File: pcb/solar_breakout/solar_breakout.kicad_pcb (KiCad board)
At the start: 2 copper layers, 20.8 x 43.7 mm, 25 parts, among them IC1 LTC3105, J1 CONN_01x02, J2 CONN_01x02, J3 CONN_01x02, J4 CONN_01x02, J5 CONN_01x02, J6 CONN_01x02

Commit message: Fix some stuff with the PCB
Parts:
- moved C6 4.84 mm to (151.3, 119.0), turned to 270 degrees
- moved G*** 4.67 mm to (145.2, 121.0)
- moved J1 4.32 mm to (148.6, 124.6)
- moved D2 3.95 mm to (143.8, 125.0), turned to 0 degrees
- moved L1 2.59 mm to (153.2, 123.2)
- moved IC1 2.52 mm to (148.0, 118.6)
- moved R1 2.33 mm to (145.3, 121.7)
- moved C2 2.25 mm to (148.9, 121.0)
- moved C5 2.16 mm to (145.3, 118.6)
- moved C3 2.09 mm to (150.2, 115.7), turned to 0 degrees
- moved C4 2.01 mm to (145.3, 116.2)
- moved R4 1.82 mm to (154.2, 111.5)
- moved J6 1.02 mm to (150.1, 111.3)
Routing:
- net /Panel_V: track 81.0 -> 60.9 mm
- net Net-(IC1-Pad7): track 7.71 -> 9.92 mm
- net GND: track 15.1 -> 17.0 mm
- net Net-(C3-Pad1): track 3.45 -> 1.94 mm
- net Net-(C4-Pad1): track 33.2 -> 34.7 mm
- net /D_anode: track 24.8 -> 23.4 mm
- net Net-(J6-Pad1): track 4.02 -> 5.45 mm
- net /Array_1_+: track 5.38 -> 4.15 mm
- net /Cap_V: track 67.1 -> 68.2 mm
- net Net-(C5-Pad1): track 1.77 -> 1.26 mm
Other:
- board size 20.8 x 43.7 mm -> 20.8 x 39 mm
- net class Power added: clearance 0.2, trace_width 0.3, via_dia 0.8, via_drill 0.4
- board text removed: "Feb 2019"
- board text removed: "Joel Mayer"
- board text removed: "Version 1"
- board text removed: "http://www.cusf.co.uk/"

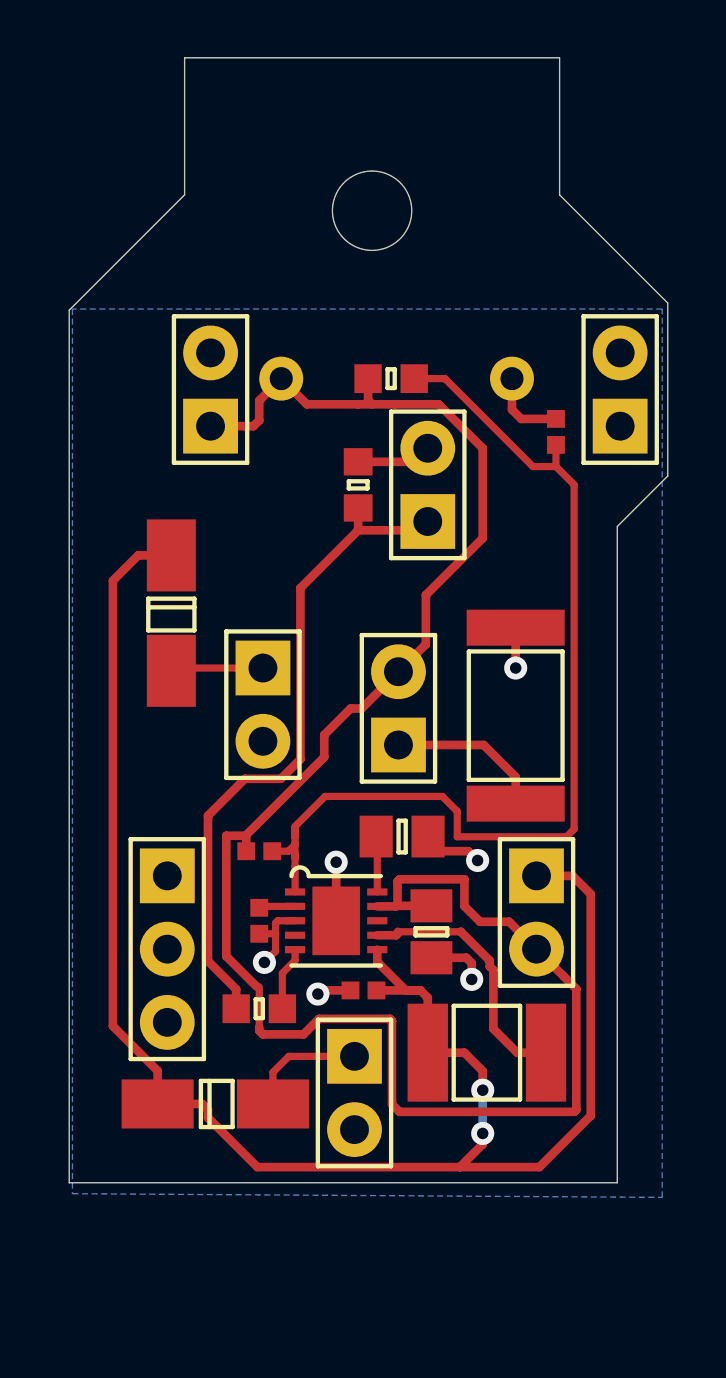
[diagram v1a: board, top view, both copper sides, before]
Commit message: Make the baord smaller and fix power lines
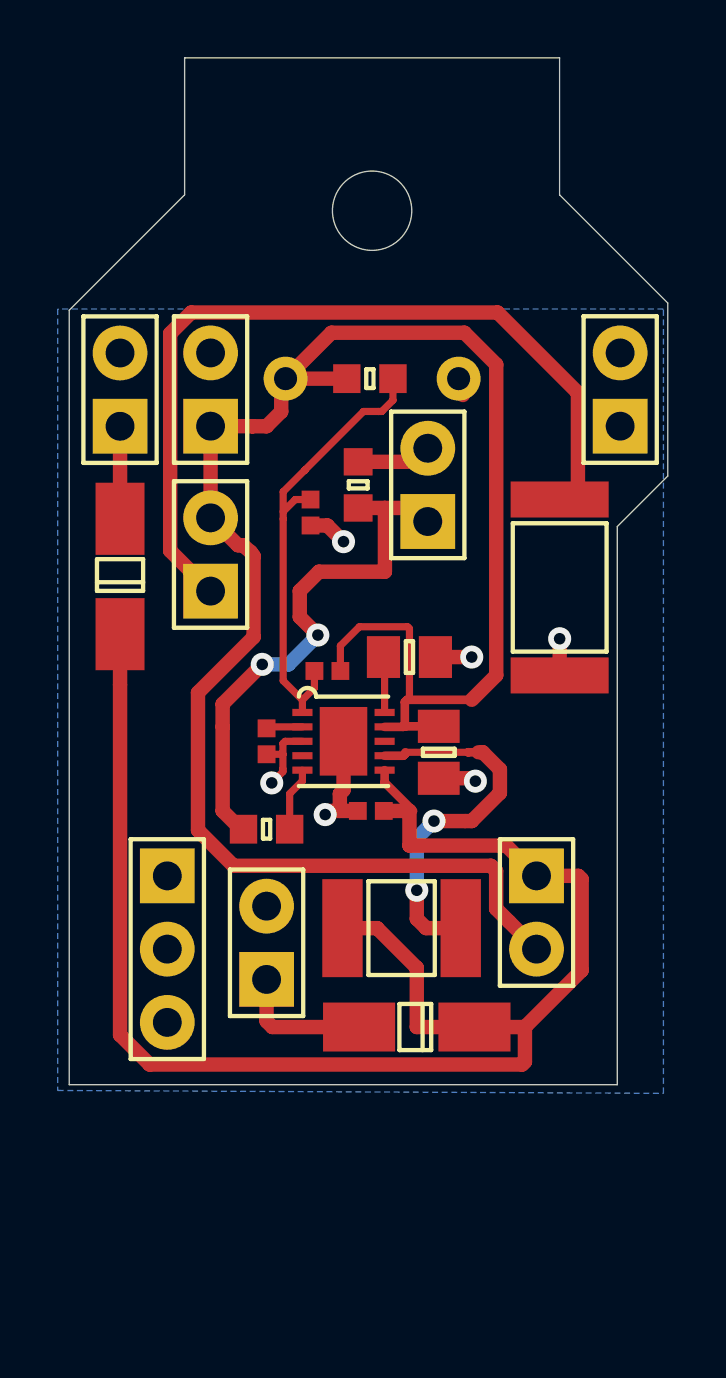
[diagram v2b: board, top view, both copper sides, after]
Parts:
- R1: value 30k -> 76.8k
- moved G*** 13.1 mm to (146.6, 108.0)
- moved J2 12.0 mm to (140.5, 100.2), turned to 90 degrees
- moved R3 8.96 mm to (147.1, 104.5), turned to 270 degrees
- moved J6 8.42 mm to (143.6, 105.9)
- moved D2 7.48 mm to (150.7, 122.3), turned to 180 degrees
- moved C4 6.68 mm to (147.7, 110.0), turned to 0 degrees
- moved C2 6.23 mm to (149.2, 114.8)
- moved C3 6.23 mm to (150.5, 109.5)
- moved C5 6.23 mm to (145.5, 112.4)
- moved C6 6.23 mm to (151.5, 112.8)
- moved IC1 6.23 mm to (148.2, 112.4)
- moved R1 6.23 mm to (145.5, 115.4)
- moved J1 6.03 mm to (145.5, 119.4), turned to 90 degrees
- moved L1 5.23 mm to (150.2, 118.9)
- moved C7 4.85 mm to (149.2, 99.8)
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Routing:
- net Net-(J6-Pad1): track 5.45 -> 28.9 mm
- net Net-(C4-Pad1): track 34.7 -> 16.1 mm
- net /Panel_V: track 60.9 -> 54.9 mm, vias 2 -> 0
- net /D_anode: track 23.4 -> 19.0 mm, vias 0 -> 2
- net Net-(IC1-Pad7): track 9.92 -> 13.1 mm, vias 0 -> 2
- net GND: track 17.0 -> 15.2 mm
- net /Cap_V: track 68.2 -> 67.2 mm
- net /Array_2_+: track 2.58 -> 3.21 mm
- net /Array_1_+: track 4.15 -> 4.74 mm
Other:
- board size 20.8 x 39 mm -> 20.8 x 35.6 mm
- net class Power: trace_width 0.3 -> 0.5
- board text added: "Feb 2019"
- board text added: "Joel Mayer"
- board text added: "http://www.cusf.co.uk/"

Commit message: Fix some traces and move connections closer to edge
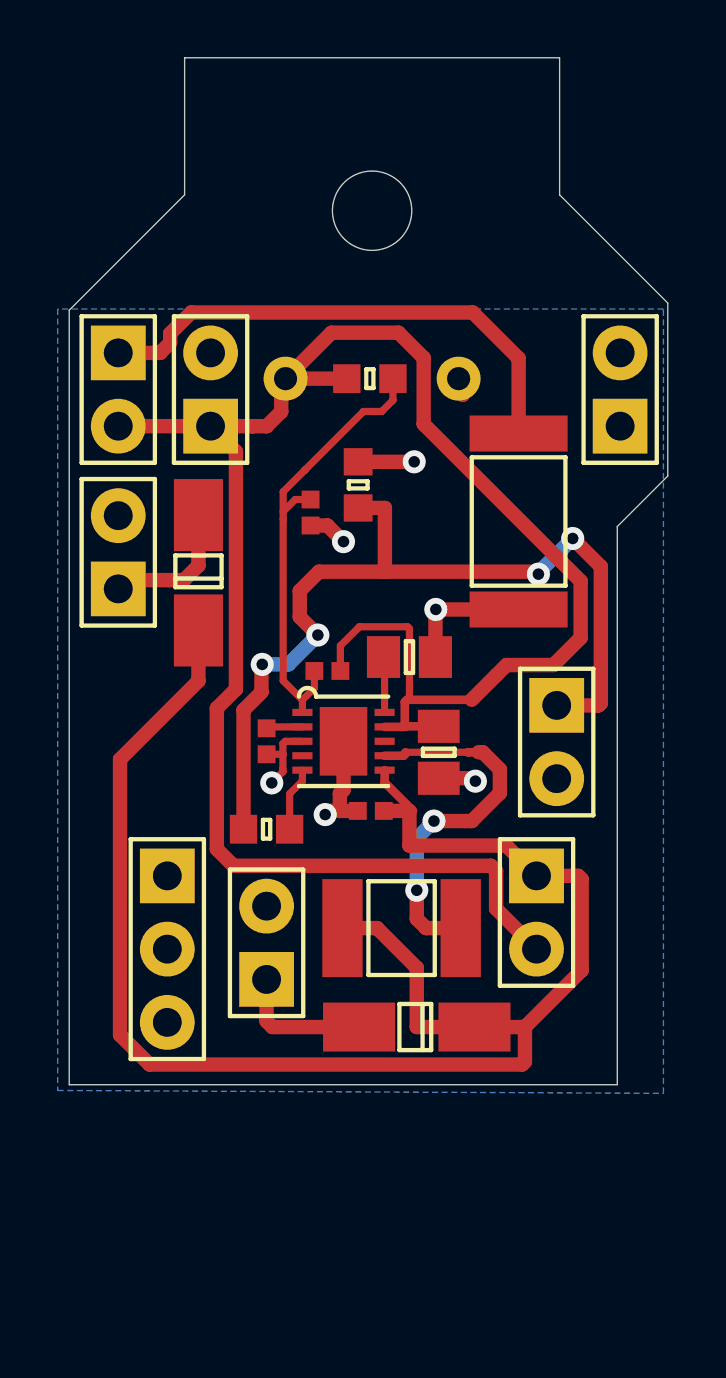
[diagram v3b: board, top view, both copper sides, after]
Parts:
- moved J3 9.97 mm to (155.6, 112.4), turned to 270 degrees
- moved G*** 9.71 mm to (155.1, 103.3)
- moved J6 6.55 mm to (140.4, 100.2), turned to 270 degrees
- moved J2 5.64 mm to (140.4, 105.8)
- moved D3 2.72 mm to (143.2, 106.6)
- moved R4 2.69 mm to (154.3, 104.8)
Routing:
- net /D_anode: track 19.0 -> 31.3 mm, vias 2 -> 4
- net Net-(J6-Pad1): track 28.9 -> 17.9 mm
- net /Cap_V: track 67.2 -> 71.3 mm
- net /Array_2_+: track 3.21 -> 5.03 mm
- net GND: track 15.2 -> 16.5 mm
- net /Panel_V: track 54.9 -> 56.1 mm
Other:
- net class Default: trace_width 0.25 -> 0.5
- rule via_min_size: 0.4 -> 0.45
- board text removed: "JUMPER"
- board text removed: "http://www.cusf.co.uk/"

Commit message: Improve routing and change resistor
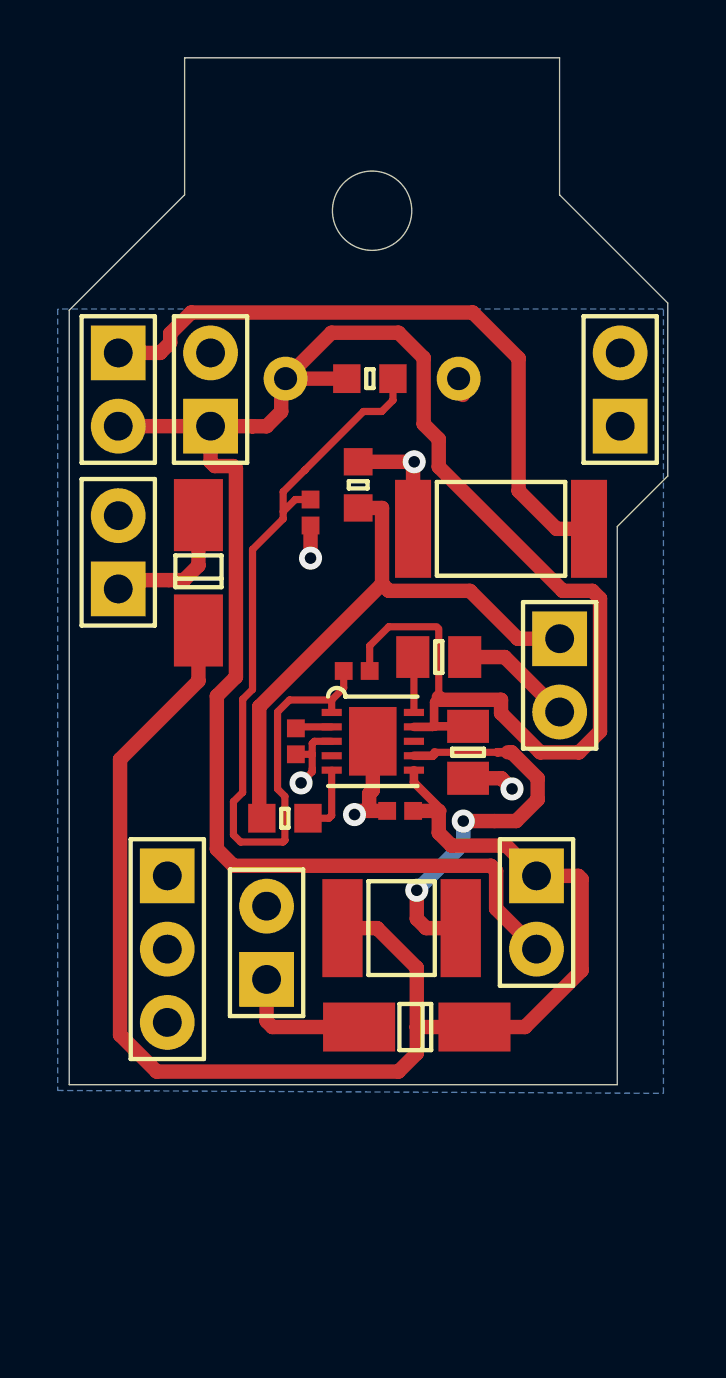
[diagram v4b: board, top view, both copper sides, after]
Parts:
- moved G*** 2.43 mm to (154.8, 100.8)
- moved J3 2.31 mm to (155.7, 110.1)
- moved C2 1.02 mm to (150.2, 114.8)
- moved C3 1.02 mm to (151.5, 109.5)
- moved C4 1.02 mm to (148.7, 110.0)
- moved C5 1.02 mm to (146.6, 112.4)
- moved C6 1.02 mm to (152.5, 112.8)
- moved IC1 1.02 mm to (149.2, 112.4)
- moved R1 0.74 mm to (146.2, 115.1)
- moved R4 0.66 mm to (153.7, 105.0), turned to 180 degrees
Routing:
- net Net-(C4-Pad1): track 16.1 -> 29.7 mm
- net /D_anode: track 31.3 -> 20.3 mm, vias 4 -> 0
- net /Cap_V: track 71.3 -> 76.7 mm
- net /Panel_V: track 56.1 -> 51.1 mm
- net Net-(J6-Pad1): track 17.9 -> 22.9 mm
- net GND: track 16.5 -> 18.5 mm, vias 6 -> 5
- net Net-(IC1-Pad7): track 13.1 -> 14.1 mm
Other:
- net class Default: trace_width 0.5 -> 0.25
- board text added: "http://www.cusf.co.uk/"

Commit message: Fix small changes to both boards
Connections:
- REF** pad 2: (no net) -> GND
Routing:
- net GND: track 18.5 -> 16.0 mm, vias 5 -> 6
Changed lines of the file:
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@@
     (thickness 1.6)
     (drawings 27)
-    (tracks 178)
+    (tracks 176)
     (zones 0)
     (modules 25)
@@
     (fp_line (start 2.54 -1.27) (end 2.54 1.27) (layer F.Fab) (width 0.01))
     (fp_line (start -2.54 -1.27) (end 2.54 -1.27) (layer F.Fab) (width 0.01))
-    (pad 2 thru_hole circle (at 1.27 0 90) (size 1.9 1.9) (drill 1) (layers *.Cu *.Mask F.SilkS))
+    (pad 2 thru_hole circle (at 1.27 0 90) (size 1.9 1.9) (drill 1) (layers *.Cu *.Mask F.SilkS)
+      (net 2 GND))
     (pad 1 thru_hole rect (at -1.27 0 90) (size 1.9 1.9) (drill 1) (layers *.Cu *.Mask F.SilkS))
     (model ${KISYS3DMOD}/Pin_Headers.3dshapes/Pin_Header_Straight_1x02.wrl
@@
   (segment (start 148.717 114.808) (end 148.59 114.935) (width 0.3) (layer F.Cu) (net 2))
   (segment (start 148.717 102.705) (end 150.66 102.705) (width 0.5) (layer F.Cu) (net 2))
-  (segment (start 149.098 114.212) (end 149.098 114.808) (width 0.5) (layer F.Cu) (net 2))
-  (segment (start 149.225 114.085) (end 149.098 114.212) (width 0.5) (layer F.Cu) (net 2))
-  (segment (start 149.225 112.395) (end 149.225 114.085) (width 0.5) (layer F.Cu) (net 2))
   (segment (start 149.722 114.808) (end 149.098 114.808) (width 0.5) (layer F.Cu) (net 2))
   (segment (start 149.098 114.808) (end 148.717 114.808) (width 0.5) (layer F.Cu) (net 2))
@@
   (via (at 147.066 106.045) (size 0.8) (drill 0.4) (layers F.Cu B.Cu) (net 2))
   (segment (start 147.066 104.913) (end 147.066 106.045) (width 0.5) (layer F.Cu) (net 2))
+  (via (at 149.225 112.395) (size 0.8) (drill 0.4) (layers F.Cu B.Cu) (net 2))
   (segment (start 150.65 113.395) (end 150.65 113.82) (width 0.3) (layer F.Cu) (net 3))
   (segment (start 154.499 122.301) (end 156.464 120.336) (width 0.5) (layer F.Cu) (net 3))

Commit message: Make some last minute changes to PCBs before sending off for manufacture
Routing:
- net GND: track 16.0 -> 23.3 mm, vias 6 -> 7
- net /Panel_V: track 51.1 -> 55.1 mm
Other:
- board text added: "VSOL"
- board text added: "www.cusf.co.uk cuspaceflight.com"
- board text removed: "VSOLAR"
- board text removed: "http://www.cusf.co.uk/"
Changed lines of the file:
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@@
-(kicad_pcb (version 20171130) (host pcbnew "(6.0.0-rc1-dev-1613-ga55d9819b)")
+(kicad_pcb (version 20171130) (host pcbnew "(5.0.0-rc3-dev)")
   (general
     (thickness 1.6)
     (drawings 27)
-    (tracks 176)
+    (tracks 184)
     (zones 0)
     (modules 25)
@@
     (zone_45_only no)
     (trace_min 0.2)
+    (segment_width 0.2)
+    (edge_width 0.05)
     (via_size 0.8)
     (via_drill 0.4)
@@
     (uvia_min_size 0.2)
     (uvia_min_drill 0.1)
-    (edge_width 0.05)
-    (segment_width 0.2)
     (pcb_text_width 0.3)
     (pcb_text_size 1.5 1.5)
@@
     )
   )
-  (gr_text http://www.cusf.co.uk/ (at 148.336 114.046) (layer B.SilkS)
+  (gr_text "www.cusf.co.uk\ncuspaceflight.com" (at 146.06016 112.43056) (layer B.SilkS)
     (effects (font (size 1 1) (thickness 0.15)) (justify mirror))
   )
@@
     (effects (font (size 1 1) (thickness 0.15)) (justify mirror))
   )
-  (gr_text "VSOLAR\n" (at 150.9 117.06) (layer B.SilkS)
+  (gr_text VSOL (at 151.7 117.06) (layer B.SilkS)
     (effects (font (size 1 1) (thickness 0.15)) (justify mirror))
   )
@@
     (effects (font (size 1 1) (thickness 0.15)) (justify mirror))
   )
+  (segment (start 145.112999 98.455221) (end 145.112999 100.767139) (width 0.25) (layer B.Cu) (net 2))
+  (segment (start 145.112999 100.767139) (end 145.56994 101.22408) (width 0.25) (layer B.Cu) (net 2))
+  (segment (start 145.27784 98.29038) (end 145.112999 98.455221) (width 0.25) (layer B.Cu) (net 2))
+  (segment (start 144.91716 98.16084) (end 144.91716 100.83546) (width 0.25) (layer B.Cu) (net 2))
+  (segment (start 144.91716 100.83546) (end 145.1864 101.1047) (width 0.25) (layer B.Cu) (net 2))
+  (segment (start 140.9573 123.59132) (end 143.12138 123.59132) (width 0.5) (layer B.Cu) (net 2))
   (segment (start 155.702 108.839) (end 154.252 108.839) (width 0.5) (layer F.Cu) (net 1))
-  (segment (start 149.544999 104.305) (end 148.717 104.305) (width 0.5) (layer F.Cu) (net 1))
-  (segment (start 149.544999 106.939813) (end 149.544999 104.305) (width 0.5) (layer F.Cu) (net 1))
-  (segment (start 145.288 111.196812) (end 149.544999 106.939813) (width 0.5) (layer F.Cu) (net 1))
   (segment (start 145.288 114.973) (end 145.288 111.196812) (width 0.5) (layer F.Cu) (net 1))
   (segment (start 145.377 115.062) (end 145.288 114.973) (width 0.5) (layer F.Cu) (net 1))
-  (segment (start 149.784187 107.179001) (end 149.544999 106.939813) (width 0.5) (layer F.Cu) (net 1))
   (segment (start 152.592001 107.179001) (end 149.784187 107.179001) (width 0.5) (layer F.Cu) (net 1))
   (segment (start 154.252 108.839) (end 152.592001 107.179001) (width 0.5) (layer F.Cu) (net 1))
+  (segment (start 148.717 107.767812) (end 148.69414 107.790672) (width 0.25) (layer F.Cu) (net 1))
+  (segment (start 148.717 104.305) (end 148.717 107.767812) (width 0.25) (layer F.Cu) (net 1))
+  (segment (start 145.288 111.196812) (end 148.69414 107.790672) (width 0.5) (layer F.Cu) (net 1))
+  (segment (start 149.305811 107.179001) (end 148.717 107.767812) (width 0.5) (layer F.Cu) (net 1))
+  (segment (start 149.784187 107.179001) (end 149.305811 107.179001) (width 0.5) (layer F.Cu) (net 1))
   (segment (start 146.558 112.845) (end 147.124 112.845) (width 0.25) (layer F.Cu) (net 2))
   (segment (start 147.2 112.395) (end 147.8 112.395) (width 0.25) (layer F.Cu) (net 2))
@@
   (via (at 148.59 114.935) (size 0.8) (drill 0.4) (layers F.Cu B.Cu) (net 2))
   (segment (start 148.717 114.808) (end 148.59 114.935) (width 0.3) (layer F.Cu) (net 2))
-  (segment (start 148.717 102.705) (end 150.66 102.705) (width 0.5) (layer F.Cu) (net 2))
   (segment (start 149.722 114.808) (end 149.098 114.808) (width 0.5) (layer F.Cu) (net 2))
   (segment (start 149.098 114.808) (end 148.717 114.808) (width 0.5) (layer F.Cu) (net 2))
   (segment (start 151.772999 100.020499) (end 151.5745 99.822) (width 0.25) (layer F.Cu) (net 2))
   (segment (start 152.348009 100.389509) (end 152.348009 99.782323) (width 0.5) (layer F.Cu) (net 2))
-  (via (at 150.66 102.705) (size 0.8) (drill 0.4) (layers F.Cu B.Cu) (net 2))
-  (segment (start 150.62 102.745) (end 150.66 102.705) (width 0.5) (layer F.Cu) (net 2))
-  (segment (start 150.62 105.029) (end 150.62 102.745) (width 0.5) (layer F.Cu) (net 2))
   (segment (start 153.797 109.474) (end 152.411 109.474) (width 0.5) (layer F.Cu) (net 2))
   (segment (start 155.702 111.379) (end 153.797 109.474) (width 0.5) (layer F.Cu) (net 2))
@@
   (segment (start 147.066 104.913) (end 147.066 106.045) (width 0.5) (layer F.Cu) (net 2))
   (via (at 149.225 112.395) (size 0.8) (drill 0.4) (layers F.Cu B.Cu) (net 2))
+  (via (at 150.15464 102.23246) (size 0.8) (drill 0.4) (layers F.Cu B.Cu) (net 2) (status 1000000))
+  (segment (start 149.6821 102.705) (end 150.15464 102.23246) (width 0.5) (layer F.Cu) (net 2) (status 1000000))
+  (segment (start 148.717 102.705) (end 149.6821 102.705) (width 0.5) (layer F.Cu) (net 2) (status 1000000))
+  (via (at 152.06218 104.96804) (size 0.8) (drill 0.4) (layers F.Cu B.Cu) (net 2))
+  (segment (start 152.00122 105.029) (end 152.06218 104.96804) (width 0.5) (layer F.Cu) (net 2))
+  (segment (start 150.62 105.029) (end 152.00122 105.029) (width 0.5) (layer F.Cu) (net 2))
   (segment (start 150.65 113.395) (end 150.65 113.82) (width 0.3) (layer F.Cu) (net 3))
-  (segment (start 154.499 122.301) (end 156.464 120.336) (width 0.5) (layer F.Cu) (net 3))
-  (segment (start 152.749 122.301) (end 154.499 122.301) (width 0.5) (layer F.Cu) (net 3))
   (segment (start 156.35 117.06) (end 154.9 117.06) (width 0.5) (layer F.Cu) (net 3))
   (segment (start 156.464 117.174) (end 156.35 117.06) (width 0.5) (layer F.Cu) (net 3))
@@
   (segment (start 140.462 122.574002) (end 141.732988 123.84499) (width 0.5) (layer F.Cu) (net 3))
   (segment (start 150.115012 123.84499) (end 150.749 123.211002) (width 0.5) (layer F.Cu) (net 3))
+  (segment (start 150.115012 123.84499) (end 154.11991 123.84499) (width 0.5) (layer F.Cu) (net 3))
+  (segment (start 156.464 121.5009) (end 156.464 120.336) (width 0.5) (layer F.Cu) (net 3))
+  (segment (start 154.11991 123.84499) (end 156.464 121.5009) (width 0.5) (layer F.Cu) (net 3))
   (segment (start 150.65 109.513) (end 150.611 109.474) (width 0.25) (layer F.Cu) (net 4))
   (segment (start 150.65 111.395) (end 150.65 109.513) (width 0.25) (layer F.Cu) (net 4))
@@
   (segment (start 156.374001 112.779001) (end 155.029999 112.779001) (width 0.5) (layer F.Cu) (net 6))
   (segment (start 144.279802 102.149802) (end 143.6 101.47) (width 0.5) (layer F.Cu) (net 6))
-  (segment (start 144.479801 110.163001) (end 144.479801 102.942999) (width 0.5) (layer F.Cu) (net 6))
   (segment (start 143.816999 110.825803) (end 144.479801 110.163001) (width 0.5) (layer F.Cu) (net 6))
   (segment (start 153.499999 118.199999) (end 153.499999 116.888997) (width 0.5) (layer F.Cu) (net 6))
@@
   (segment (start 144.395999 116.709999) (end 143.816999 116.130999) (width 0.5) (layer F.Cu) (net 6))
   (segment (start 143.816999 116.130999) (end 143.816999 110.825803) (width 0.5) (layer F.Cu) (net 6))
-  (segment (start 144.389801 102.852999) (end 143.746999 102.852999) (width 0.5) (layer F.Cu) (net 6))
-  (segment (start 144.479801 102.942999) (end 144.389801 102.852999) (width 0.5) (layer F.Cu) (net 6))
-  (segment (start 143.6 102.706) (end 143.6 101.47) (width 0.5) (layer F.Cu) (net 6))
-  (segment (start 143.746999 102.852999) (end 143.6 102.706) (width 0.5) (layer F.Cu) (net 6))
   (segment (start 151.595696 110.955696) (end 151.511 110.871) (width 0.5) (layer F.Cu) (net 6))
   (segment (start 153.67 110.955696) (end 151.595696 110.955696) (width 0.5) (layer F.Cu) (net 6))
+  (segment (start 145.542 102.615521) (end 144.479801 103.67772) (width 0.5) (layer F.Cu) (net 6))
+  (segment (start 145.542 101.473) (end 145.542 102.615521) (width 0.5) (layer F.Cu) (net 6))
+  (segment (start 144.479801 110.163001) (end 144.479801 103.67772) (width 0.5) (layer F.Cu) (net 6))
   (segment (start 146.608 111.895) (end 146.558 111.945) (width 0.25) (layer F.Cu) (net 7))
   (segment (start 147.8 111.895) (end 146.608 111.895) (width 0.25) (layer F.Cu) (net 7))
